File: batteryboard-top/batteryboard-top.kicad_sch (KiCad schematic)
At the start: 6 parts, among them J1 FLE-105-01-G-DV-A, J2 FLE-105-01-G-DV-A

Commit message: Some changes
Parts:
- removed J1: FLE-105-01-G-DV-A, batteryboard:SAMTEC_FLE-105-01-G-DV-A, symbol Connector_Generic:Conn_02x05_Odd_Even
- added J1: FLE-107-01-G-DV-A, batteryboard:SAMTEC_FLE-107-01-G-DV-A, symbol Connector_Generic:Conn_02x07_Odd_Even
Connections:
- net SCL3 is gone; now on net BATT_P: J2.6 (Pin_6)
- net +3V3: now also J2.2 (Pin_2), J1.3 (Pin_3), J1.5 (Pin_5); no longer J2.3 (Pin_3)
- net BATT_P: now also J2.4 (Pin_4), J1.7 (Pin_7), J1.9 (Pin_9); no longer J2.9 (Pin_9)
- net GND: now also J2.1 (Pin_1), J2.3 (Pin_3), J1.1 (Pin_1), J1.2 (Pin_2); no longer J2.4 (Pin_4)
- net COIL_N renamed SCL1
- net SCL1: now also J1.11 (Pin_11)
- net COIL_P renamed COIL5_P
- net COIL5_P: now also J1.12 (Pin_12)
- net SDA3: no longer names the net of J2.5 (Pin_5)
- net VBUS renamed SDA1
- net SDA1: now also J1.13 (Pin_13)
- new net COIL5_N: J1.14 (Pin_14), J2.9 (Pin_9)
- no-connect marks 4 -> 5
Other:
- moved on the sheet: J2

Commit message: B2/01 Updates
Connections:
- net +3V3: now also J1.7 (Pin_7); no longer J1.3 (Pin_3)
- net BATT_P: now also J1.10 (Pin_10), J1.12 (Pin_12); no longer J1.7 (Pin_7), J1.9 (Pin_9)
- net COIL5_N: now also J2.7 (Pin_7); no longer J2.9 (Pin_9)
- net COIL5_P: now also J1.13 (Pin_13), J2.9 (Pin_9); no longer J1.12 (Pin_12), J2.7 (Pin_7)
- net GND: now also J1.3 (Pin_3); no longer J1.2 (Pin_2)
- net SCL1: now also J1.9 (Pin_9); no longer J1.11 (Pin_11)
- net SDA1: now also J1.11 (Pin_11); no longer J1.13 (Pin_13)
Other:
- note added: "To +Y Solar Panel"
- note removed: "+Y Solar Conn"
- note removed: "Grounded Mounting Holes"
- moved on the sheet: J2

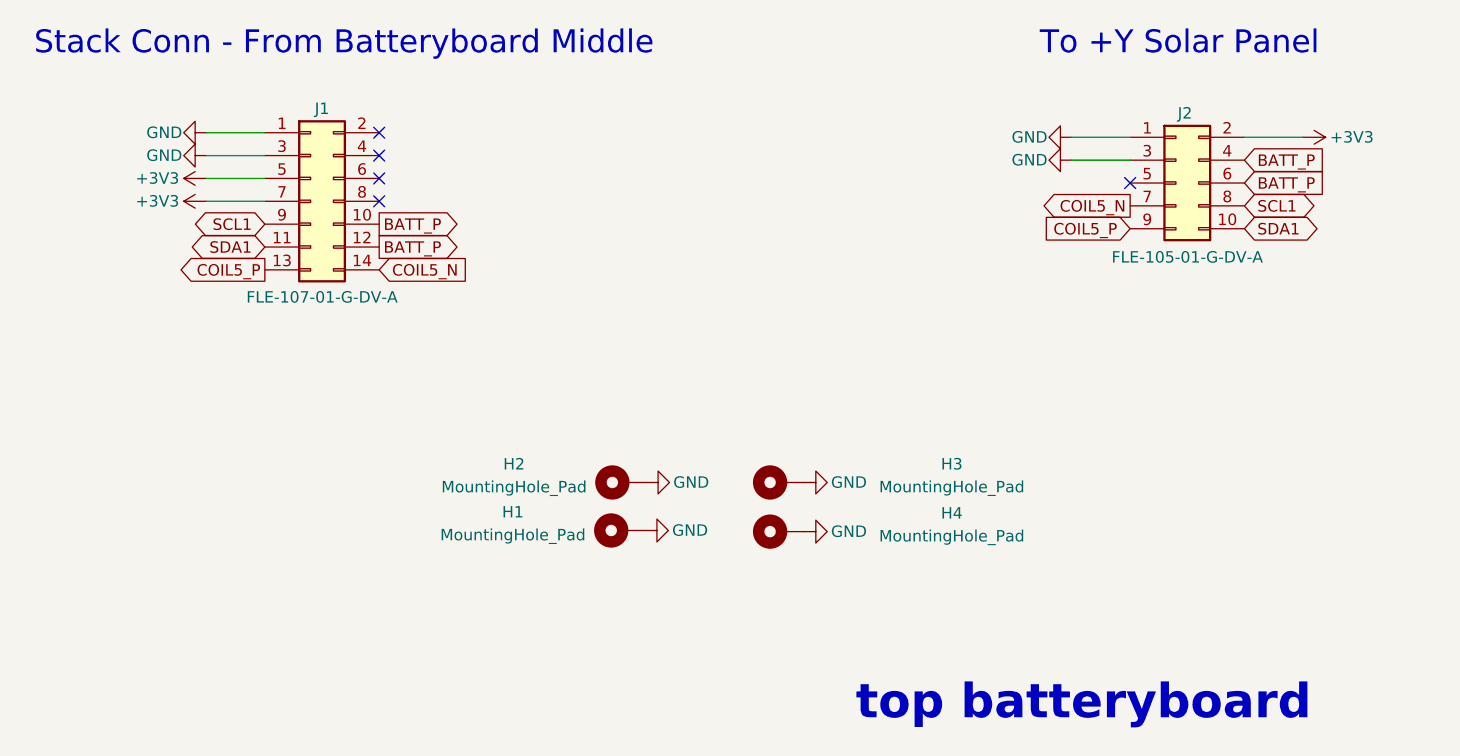
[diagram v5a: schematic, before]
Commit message: Updated batteryboards for Rev B3/01
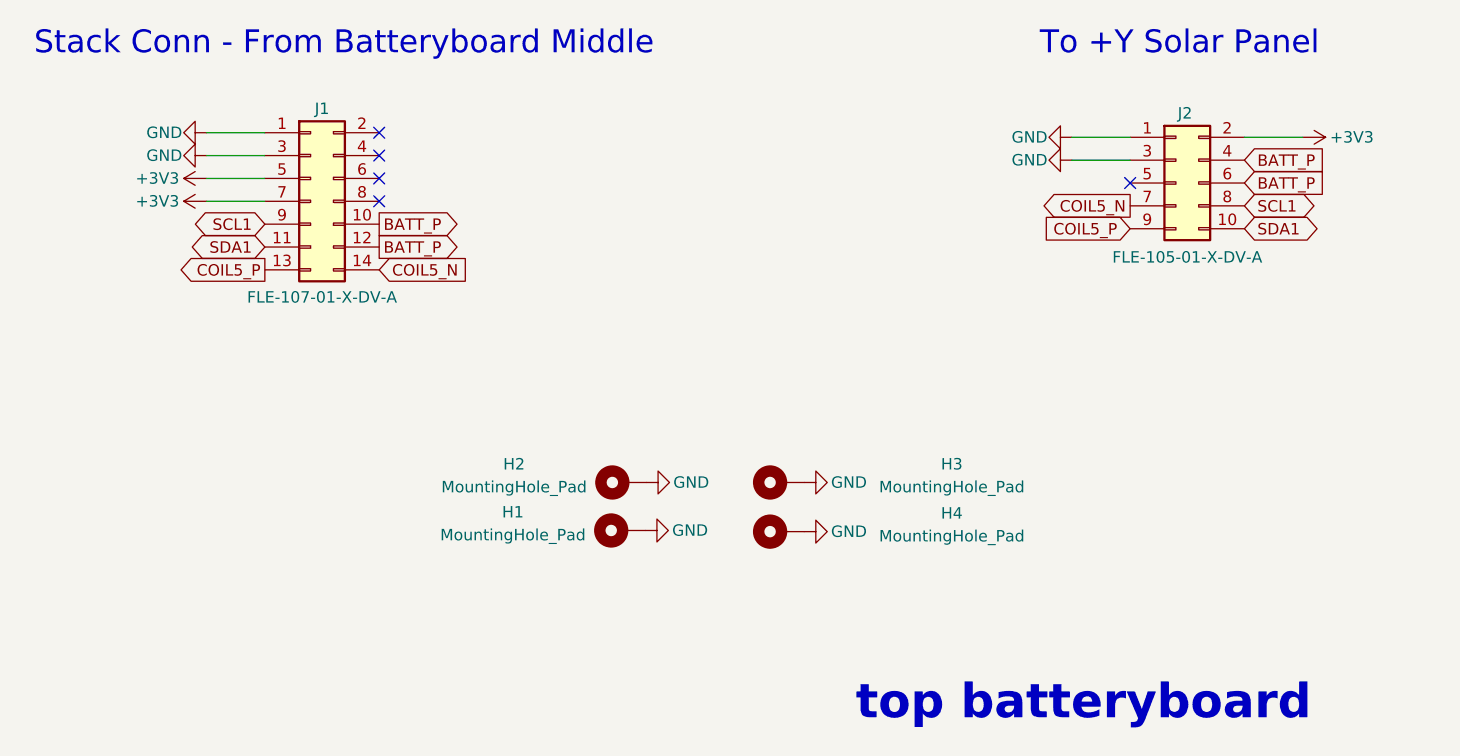
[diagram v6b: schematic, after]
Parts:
- J1: value FLE-107-01-G-DV-A -> FLE-107-01-X-DV-A; footprint batteryboard:SAMTEC_FLE-107-01-G-DV-A -> batteryboard:SAMTEC_FLE-107-01-X-DV-A
- J2: value FLE-105-01-G-DV-A -> FLE-105-01-X-DV-A; footprint batteryboard:SAMTEC_FLE-105-01-G-DV-A -> batteryboard:SAMTEC_FLE-105-01-X-DV-A

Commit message: Rev B3/02 updates
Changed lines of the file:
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@@
   (title_block
     (title "PyCubed Mini")
-    (date "2023-02-18")
-    (rev "B3/01")
+    (date "2023-04-12")
+    (rev "B3/02")
     (company "RExLab Carnegie Mellon University")
     (comment 1 "N. Khera")
@@
     (effects (font (size 2.54 2.54)) (justify left bottom))
   )
-  (text "top batteryboard" (at 122.174 115.062 0)
+  (text "top batteryboard" (at 121.285 113.792 0)
     (effects (font (size 3.81 3.81) (thickness 1.016) bold) (justify left bottom))
   )

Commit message: Updated BOMs and STEP files
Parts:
- H1, H2, H3, H4: now left out of the parts list
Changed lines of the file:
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@@
   )
   (symbol (lib_id "Mechanical:MountingHole_Pad") (at 96.266 93.599 90) (unit 1)
-    (in_bom yes) (on_board yes) (dnp no)
+    (in_bom no) (on_board yes) (dnp no)
     (property "Reference" "H1" (at 84.074 91.567 90)
       (effects (font (size 1.27 1.27)))
@@
   )
   (symbol (lib_id "Mechanical:MountingHole_Pad") (at 113.919 88.265 90) (unit 1)
-    (in_bom yes) (on_board yes) (dnp no)
+    (in_bom no) (on_board yes) (dnp no)
     (property "Reference" "H3" (at 132.842 86.233 90)
       (effects (font (size 1.27 1.27)))
@@
   )
   (symbol (lib_id "Mechanical:MountingHole_Pad") (at 113.919 93.726 90) (unit 1)
-    (in_bom yes) (on_board yes) (dnp no)
+    (in_bom no) (on_board yes) (dnp no)
     (property "Reference" "H4" (at 132.842 91.694 90)
       (effects (font (size 1.27 1.27)))
@@
   )
   (symbol (lib_id "Mechanical:MountingHole_Pad") (at 96.393 88.265 90) (unit 1)
-    (in_bom yes) (on_board yes) (dnp no)
+    (in_bom no) (on_board yes) (dnp no)
     (property "Reference" "H2" (at 84.201 86.2361 90)
       (effects (font (size 1.27 1.27)))
